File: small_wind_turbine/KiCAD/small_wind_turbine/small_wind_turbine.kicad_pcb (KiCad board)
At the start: 2 copper layers, 90 x 90 mm, 94 parts, among them J1 Conn_01x03_Male, J2 Conn_01x03_Male, J3 Conn_01x03_Male, K1 G5LE-1, Q1 Q_NMOS_GDS, SW1 SW_Push_SPDT, U10 AZ1117-5.0, U2 UC2844A, U3 LTC4440ES6, U4 Opamp_Quad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

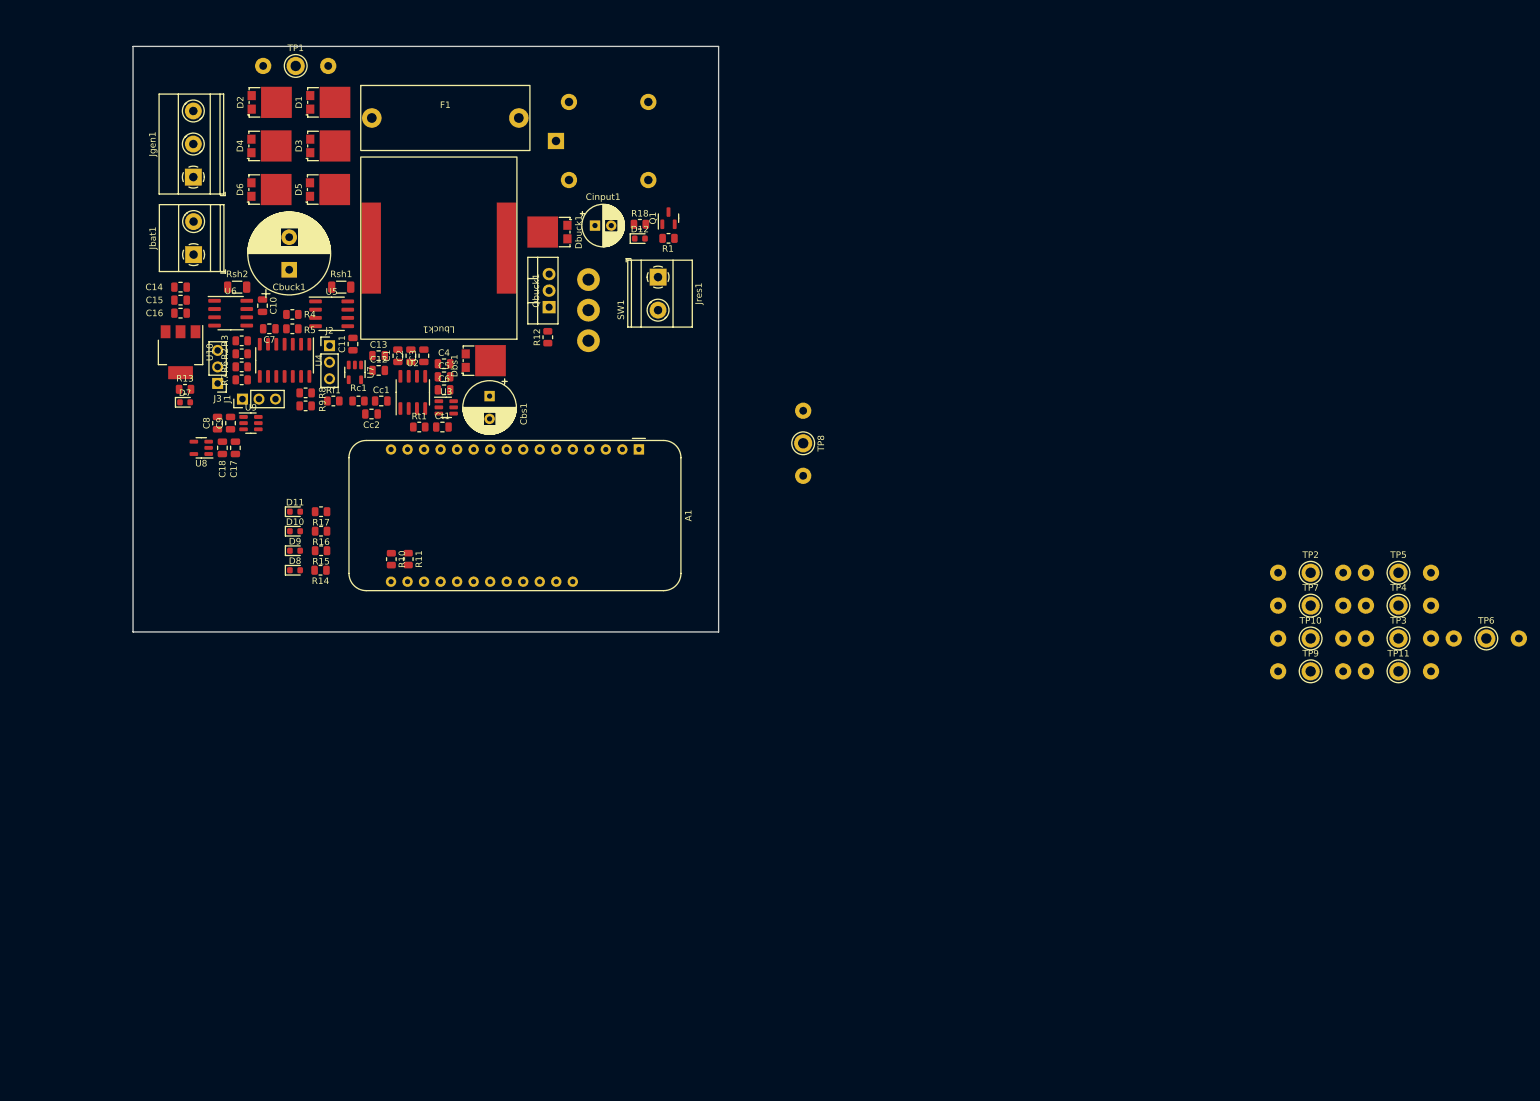
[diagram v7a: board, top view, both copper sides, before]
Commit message: move test points close to proper locations
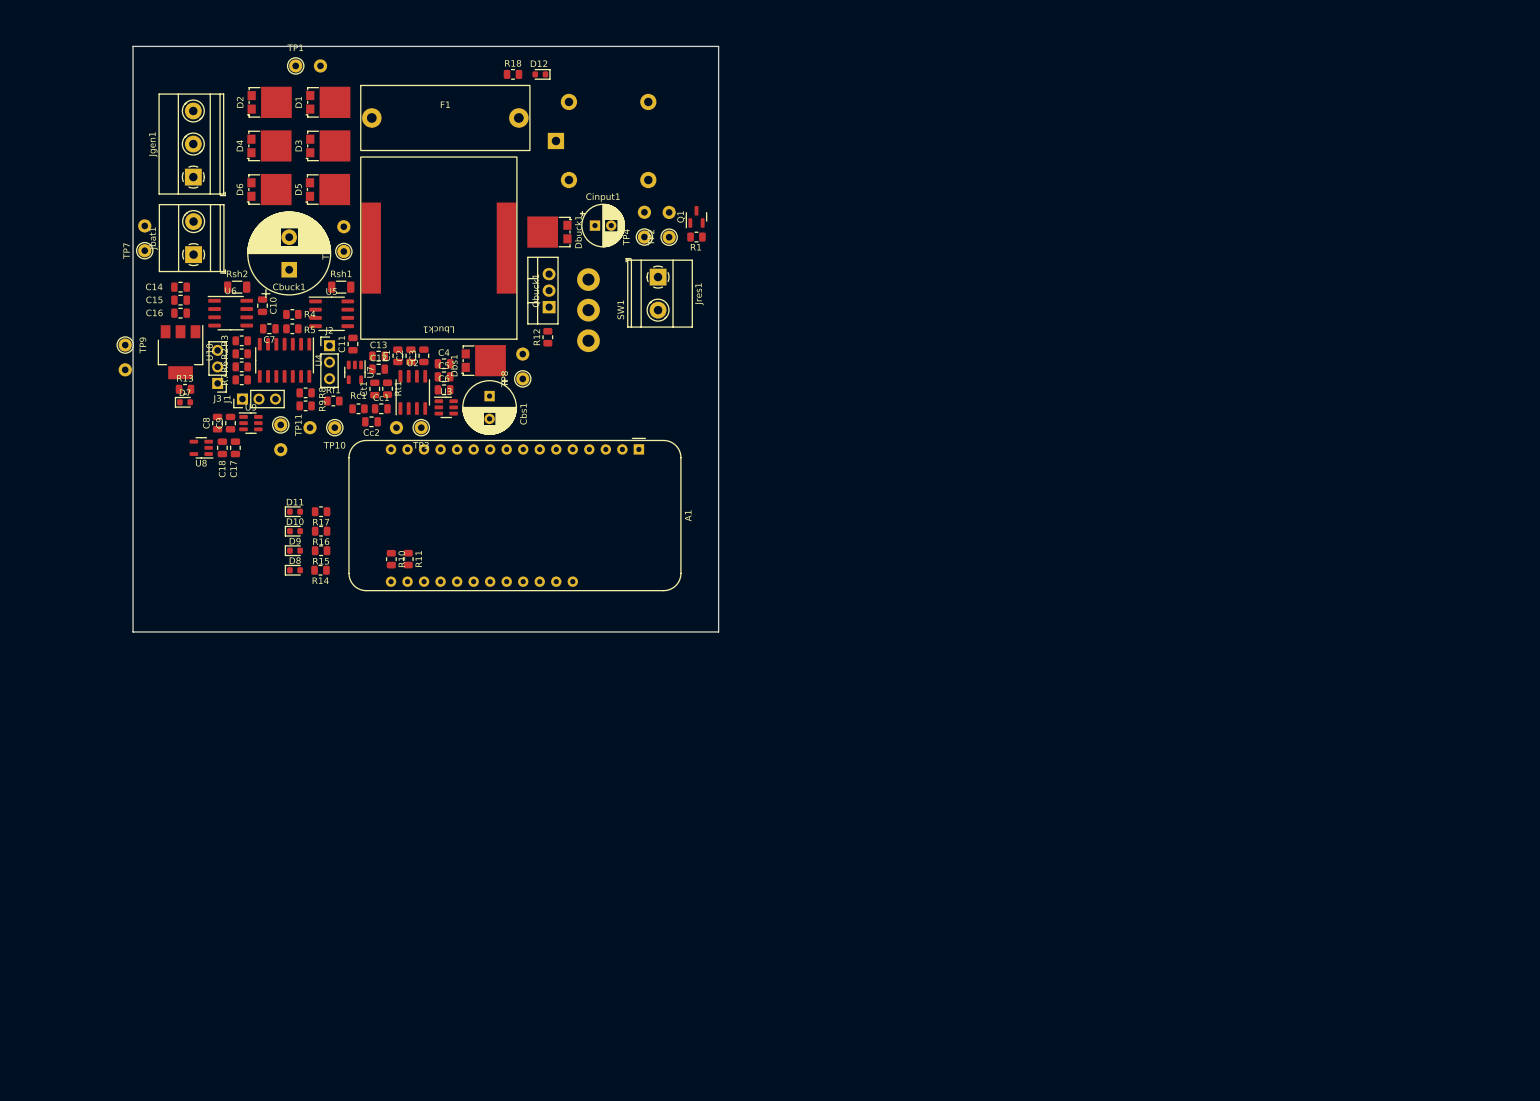
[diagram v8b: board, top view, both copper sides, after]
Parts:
- removed TP5: TestPoint_2Pole, small_wind_turbine:Oscilloscope_Test_Point
- moved TP9 189.0 mm to (39.8, 76.9), turned to -90 degrees
- moved TP7 187.3 mm to (42.8, 62.4), turned to 90 degrees
- moved TP6 185.4 mm to (73.4, 62.5), turned to 90 degrees
- moved TP11 175.9 mm to (63.7, 89.2), turned to -90 degrees
- moved TP3 153.7 mm to (85.3, 89.6), turned to 180 degrees
- moved TP10 153.4 mm to (72.0, 89.6), turned to 180 degrees
- moved TP4 129.0 mm to (119.6, 60.3), turned to 90 degrees
- moved TP2 111.3 mm to (123.4, 60.3), turned to 90 degrees
- moved TP8 44.2 mm to (100.9, 82.1), turned to 90 degrees
- moved R18 30.2 mm to (99.4, 35.3)
- moved D12 29.5 mm to (103.6, 35.3), turned to 180 degrees
- moved Ct1 11.9 mm to (78.2, 83.7), turned to 90 degrees
- moved Rt1 7.64 mm to (80.1, 83.6), turned to -90 degrees
- moved R1 4.30 mm to (127.6, 60.3)
- moved Q1 4.30 mm to (127.6, 57.2)
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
